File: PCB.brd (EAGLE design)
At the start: 127 x 44.5 mm, 43 parts, among them IC1 PIC16F1826/27SO, IC2 MAX3467CPA, U1 +12v, Y1 ASL-16.000MHZ-L-C-S-50-T

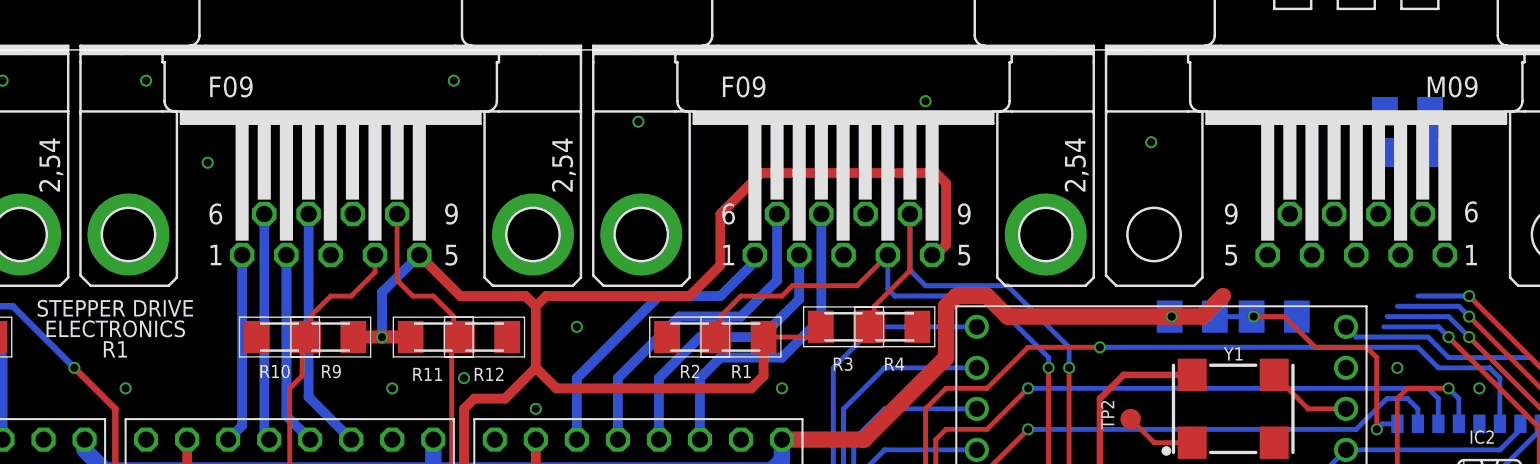
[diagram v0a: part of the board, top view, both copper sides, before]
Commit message: Switching to make D9 for power input
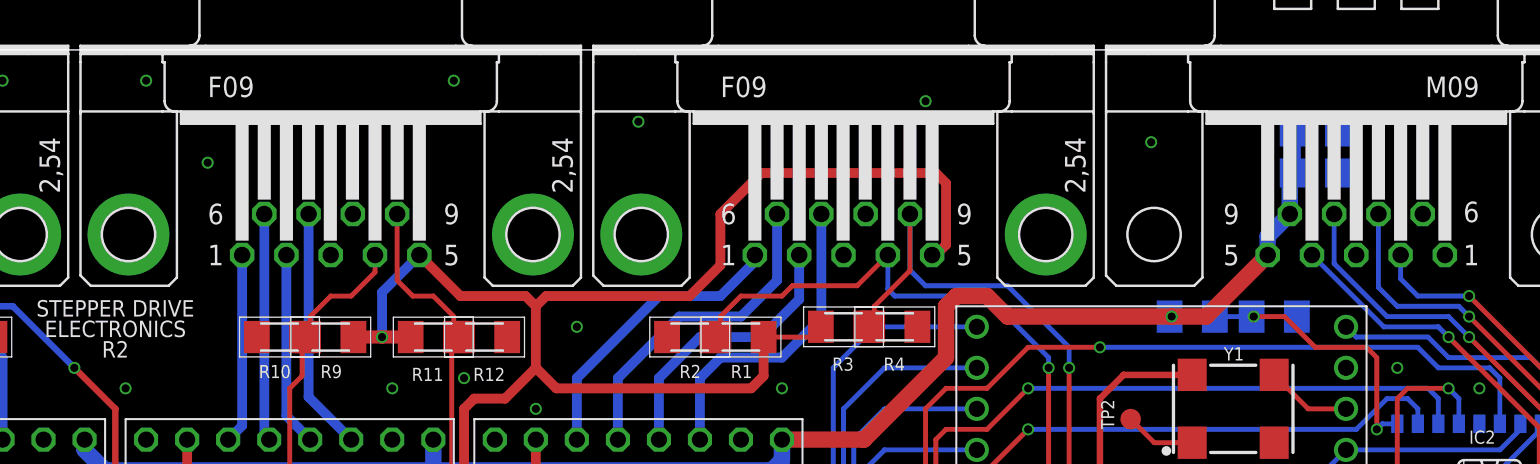
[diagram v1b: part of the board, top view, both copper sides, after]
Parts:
- moved C3 5.85 mm to (108.6, 39.4), turned to 180 degrees
- moved C4 5.85 mm to (108.6, 36.8), turned to 180 degrees
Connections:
- net RXN: now also X4.8; no longer X4.7
- net RXP: now also X4.4; no longer X4.2
- net TXN: now also X4.7; no longer X4.8
- net TXP: now also X4.2; no longer X4.4
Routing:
- net VCC: track 118.8 -> 128.3 mm
- net RXN: track 21.7 -> 29.4 mm
- net RXP: track 14.9 -> 21.1 mm
- net TXN: track 23.9 -> 30.1 mm
- net TXP: track 23.1 -> 26.1 mm
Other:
- board text added: "R2"
- board text removed: "R1"
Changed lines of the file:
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@@
 <text x="34.29" y="27.94" size="1.016" layer="21" font="fixed" align="bottom-center">STEPPER DRIVE</text>
 <text x="34.29" y="26.67" size="1.016" layer="21" font="fixed" align="bottom-center">ELECTRONICS</text>
-<text x="34.29" y="25.4" size="1.016" layer="21" font="fixed" align="bottom-center">R1</text>
+<text x="34.29" y="25.4" size="1.016" layer="21" font="fixed" align="bottom-center">R2</text>
 </plain>
 <attributes>
@@
 <attribute name="PROD_ID" value="CONN-08438" x="10.795" y="3.175" size="0.8128" layer="27" font="fixed" rot="R90" display="off"/>
 </element>
-<element name="C3" library="resistor" package="C1206" value="" x="114.3" y="40.64" rot="MR0"/>
-<element name="C4" library="resistor" package="C1206" value="" x="114.3" y="38.1" rot="MR0"/>
+<element name="C3" library="resistor" package="C1206" value="" x="108.585" y="39.37" rot="MR180"/>
+<element name="C4" library="resistor" package="C1206" value="" x="108.585" y="36.83" rot="MR180"/>
 <element name="C5" library="resistor" package="C1206" value="" x="5.08" y="12.7" rot="MR180"/>
 <element name="C6" library="resistor" package="C1206" value="" x="5.08" y="10.16" rot="MR180"/>
@@
 <wire x1="75.565" y1="19.05" x2="75.565" y2="20.32" width="1.016" layer="16"/>
 <wire x1="53.975" y1="20.32" x2="53.975" y2="18.415" width="1.016" layer="16"/>
-<wire x1="102.87" y1="29.21" x2="101.6" y2="27.94" width="1.016" layer="1"/>
 <wire x1="89.535" y1="27.94" x2="88.265" y2="29.21" width="1.016" layer="1"/>
 <wire x1="88.265" y1="29.21" x2="86.36" y2="29.21" width="1.016" layer="1"/>
@@
 <contactref element="C3" pad="1"/>
 <contactref element="C4" pad="1"/>
-<wire x1="115.7" y1="40.64" x2="115.7" y2="38.1" width="1.016" layer="16"/>
+<wire x1="107.185" y1="39.37" x2="107.185" y2="36.83" width="1.016" layer="16"/>
 <contactref element="R14" pad="2"/>
 <via x="99.695" y="27.94" extent="1-16" drill="0.5"/>
-<wire x1="99.695" y1="27.94" x2="101.6" y2="27.94" width="1.016" layer="1"/>
+<wire x1="99.695" y1="27.94" x2="101.8286" y2="27.94" width="1.016" layer="1"/>
 <wire x1="99.565" y1="27.94" x2="99.695" y2="27.94" width="1.016" layer="16"/>
 <wire x1="99.695" y1="27.94" x2="89.535" y2="27.94" width="1.016" layer="1"/>
-<wire x1="107.0102" y1="34.29" x2="115.7" y2="38.1" width="0" layer="19" extent="16-16"/>
-<wire x1="105.6386" y1="31.75" x2="107.0102" y2="34.29" width="0" layer="19" extent="1-1"/>
-<wire x1="102.87" y1="29.21" x2="105.6386" y2="31.75" width="0" layer="19" extent="1-1"/>
+<wire x1="107.0102" y1="34.29" x2="107.0102" y2="36.6552" width="1.016" layer="16"/>
+<wire x1="107.0102" y1="36.6552" x2="107.185" y2="36.83" width="1.016" layer="16"/>
+<wire x1="105.6386" y1="31.75" x2="105.6386" y2="32.9184" width="1.016" layer="16"/>
+<wire x1="105.6386" y1="32.9184" x2="107.0102" y2="34.29" width="1.016" layer="16"/>
+<wire x1="101.8286" y1="27.94" x2="105.6386" y2="31.75" width="1.016" layer="1"/>
 </signal>
 <signal name="SCK">
@@
 <signal name="RXP">
 <contactref element="IC2" pad="8"/>
-<contactref element="X4" pad="2"/>
 <wire x1="122.4534" y1="18.415" x2="122.4534" y2="21.0566" width="0.3048" layer="1"/>
 <wire x1="122.4534" y1="21.0566" x2="116.84" y2="26.67" width="0.3048" layer="1"/>
@@
 <wire x1="116.84" y1="26.67" x2="116.205" y2="27.305" width="0.3048" layer="16"/>
 <wire x1="116.205" y1="27.305" x2="112.8268" y2="27.305" width="0.3048" layer="16"/>
-<wire x1="112.8268" y1="27.305" x2="113.8682" y2="31.75" width="0" layer="19" extent="16-16"/>
+<contactref element="X4" pad="4"/>
+<wire x1="108.3818" y1="31.75" x2="112.8268" y2="27.305" width="0.3048" layer="16"/>
 </signal>
 <signal name="RXN">
 <contactref element="IC2" pad="7"/>
-<contactref element="X4" pad="7"/>
 <wire x1="122.4534" y1="17.145" x2="123.825" y2="17.145" width="0.3048" layer="1"/>
 <wire x1="123.825" y1="17.145" x2="124.46" y2="17.78" width="0.3048" layer="1"/>
@@
 <wire x1="122.4534" y1="17.145" x2="121.0564" y2="17.145" width="0.3048" layer="1"/>
 <wire x1="121.0564" y1="17.145" x2="120.4214" y2="17.78" width="0.3048" layer="1"/>
-<wire x1="113.03" y1="27.94" x2="112.4966" y2="34.29" width="0" layer="19" extent="16-16"/>
+<contactref element="X4" pad="8"/>
+<wire x1="109.7534" y1="34.29" x2="109.7534" y2="31.2166" width="0.3048" layer="16"/>
+<wire x1="109.7534" y1="31.2166" x2="113.03" y2="27.94" width="0.3048" layer="16"/>
 </signal>
 <signal name="TXN">
 <contactref element="IC2" pad="6"/>
-<contactref element="X4" pad="8"/>
 <wire x1="122.4534" y1="15.875" x2="123.825" y2="15.875" width="0.3048" layer="1"/>
 <wire x1="123.825" y1="15.875" x2="125.095" y2="17.145" width="0.3048" layer="1"/>
@@
 <wire x1="122.4534" y1="15.875" x2="121.0564" y2="15.875" width="0.3048" layer="1"/>
 <wire x1="121.0564" y1="15.875" x2="120.4214" y2="15.24" width="0.3048" layer="1"/>
-<wire x1="113.665" y1="28.575" x2="109.7534" y2="34.29" width="0" layer="19" extent="16-16"/>
+<contactref element="X4" pad="7"/>
+<wire x1="112.4966" y1="34.29" x2="112.4966" y2="29.7434" width="0.3048" layer="16"/>
+<wire x1="112.4966" y1="29.7434" x2="113.665" y2="28.575" width="0.3048" layer="16"/>
 </signal>
 <signal name="TXP">
 <contactref element="IC2" pad="5"/>
-<contactref element="X4" pad="4"/>
 <wire x1="122.4534" y1="14.605" x2="123.825" y2="14.605" width="0.3048" layer="1"/>
 <wire x1="123.825" y1="14.605" x2="125.73" y2="16.51" width="0.3048" layer="1"/>
@@
 <via x="118.11" y="29.21" extent="1-16" drill="0.5"/>
 <wire x1="118.11" y1="29.21" x2="114.935" y2="29.21" width="0.3048" layer="16"/>
-<wire x1="114.935" y1="29.21" x2="108.3818" y2="31.75" width="0" layer="19" extent="16-16"/>
+<contactref element="X4" pad="2"/>
+<wire x1="113.8682" y1="31.75" x2="113.8682" y2="30.2768" width="0.3048" layer="16"/>
+<wire x1="113.8682" y1="30.2768" x2="114.935" y2="29.21" width="0.3048" layer="16"/>
 </signal>
 <signal name="N$29">

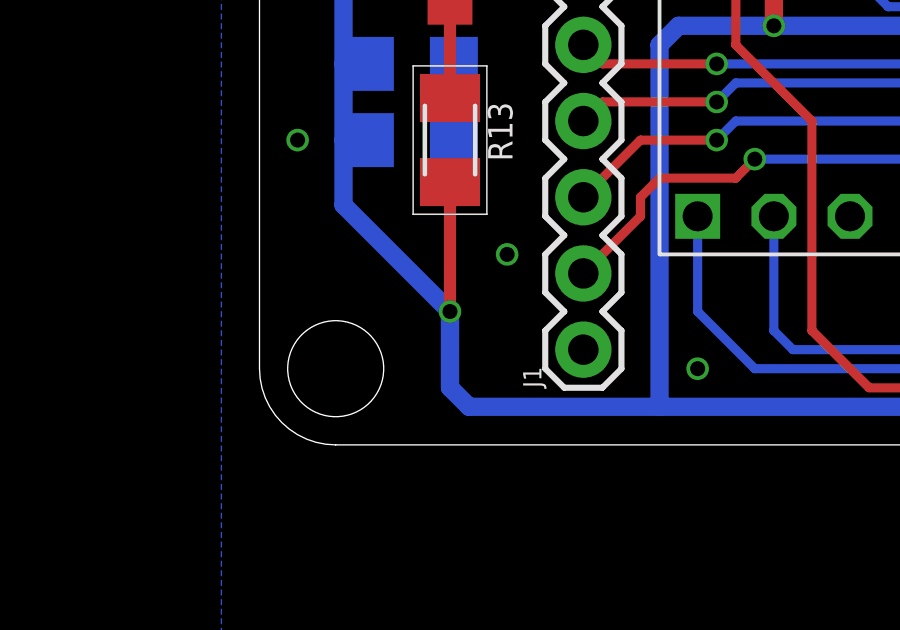
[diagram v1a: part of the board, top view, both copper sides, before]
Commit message: Adding 5V TP
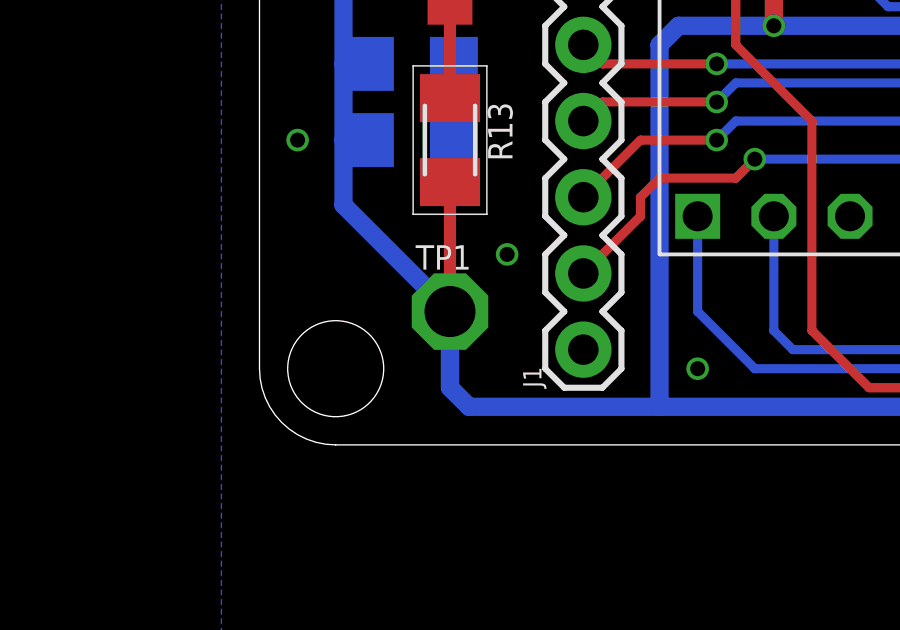
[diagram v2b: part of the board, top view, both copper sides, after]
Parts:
- added TP1: PTR1PAD1-17, testpad:P1-17
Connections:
- net +5V: now also TP1.TP
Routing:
- net +5V: vias 9 -> 8
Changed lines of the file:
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@@
 <attribute name="VALUE" x="107.315" y="25.4" size="1.27" layer="28" rot="MR0"/>
+</element>
+<element name="TP1" library="testpad" package="P1-17" value="PTR1PAD1-17" x="6.35" y="4.445" smashed="yes">
+<attribute name="TP_SIGNAL_NAME" value="" x="5.08" y="1.27" size="1" layer="37"/>
+<attribute name="NAME" x="5.207" y="5.842" size="0.8128" layer="25" font="fixed" ratio="10"/>
+<attribute name="VALUE" x="6.35" y="4.445" size="0.0254" layer="27"/>
 </element>
 </elements>
@@
 <wire x1="2.8" y1="10.16" x2="2.8" y2="7.995" width="0.6096" layer="16"/>
 <wire x1="2.8" y1="7.995" x2="6.35" y2="4.445" width="0.6096" layer="16"/>
-<wire x1="6.35" y1="4.445" x2="6.35" y2="3.175" width="0.6096" layer="16"/>
-<wire x1="6.35" y1="3.175" x2="6.35" y2="1.905" width="0.6096" layer="16"/>
+<wire x1="6.35" y1="4.445" x2="6.35" y2="1.905" width="0.6096" layer="16"/>
 <wire x1="6.35" y1="1.905" x2="6.985" y2="1.27" width="0.6096" layer="16"/>
 <wire x1="17.145" y1="13.97" x2="13.97" y2="13.97" width="0.6096" layer="16"/>
@@
 <contactref element="R13" pad="2"/>
 <wire x1="6.35" y1="8.76" x2="6.35" y2="4.445" width="0.4064" layer="1"/>
-<via x="6.35" y="4.445" extent="1-16" drill="0.5"/>
+<contactref element="TP1" pad="TP"/>
 </signal>
 <signal name="N$7">

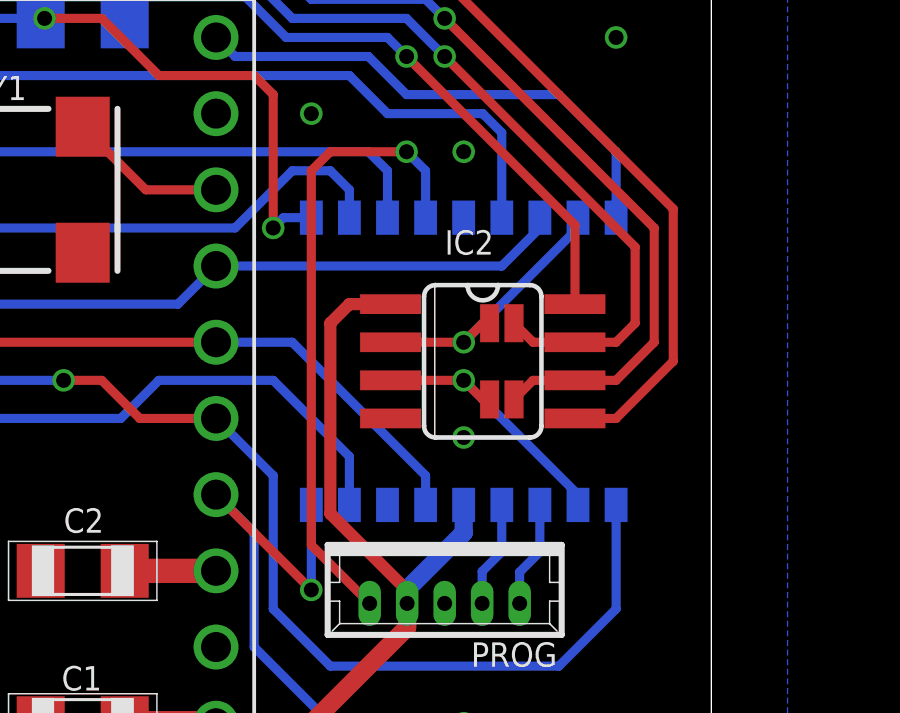
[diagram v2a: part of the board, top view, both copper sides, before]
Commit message: Adding PIC test point
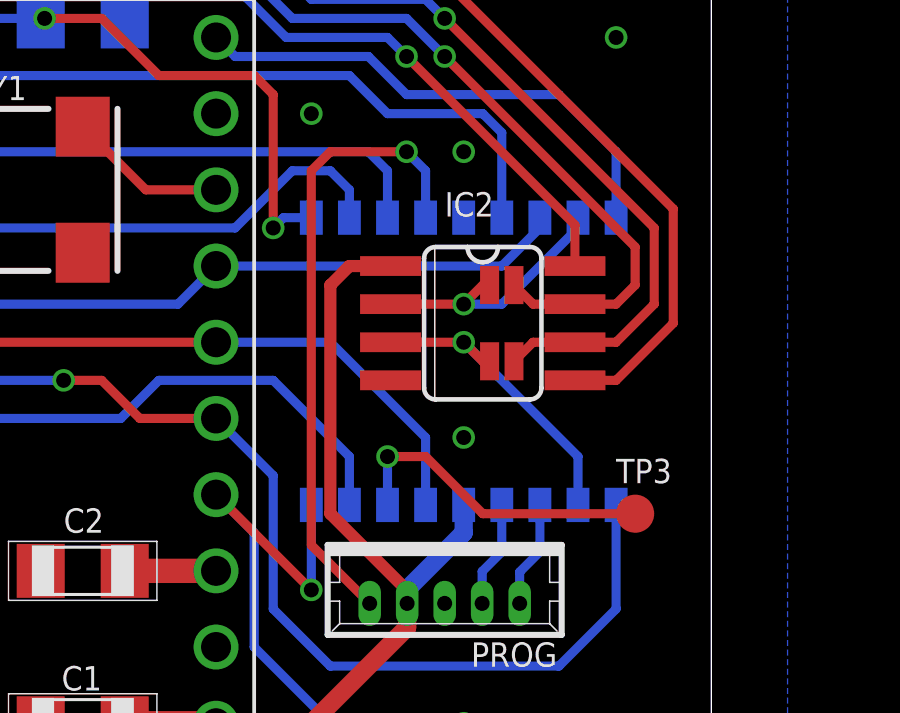
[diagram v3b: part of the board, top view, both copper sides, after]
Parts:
- added TP3: PTR1B1,27, testpad:B1,27
- moved JP1 1.27 mm to (120.0, 16.5)
- moved IC2 1.27 mm to (119.4, 17.8)
- moved JP2 1.27 mm to (120.0, 19.1)
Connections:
- new net N$25: IC1.16, TP3.TP
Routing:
- net N$25: track 0.00 -> 10.7 mm, vias 0 -> 1
- net UARTTX: track 9.30 -> 10.6 mm
- net TXP: track 26.1 -> 24.8 mm
- net TXN: track 30.1 -> 28.8 mm
- net RXP: track 21.1 -> 19.9 mm
- net RXN: track 29.4 -> 28.1 mm
- net +5V: track 384.2 -> 385.5 mm
- net MOSI: track 136.5 -> 137.2 mm
- net UARTRX: track 9.30 -> 8.77 mm
